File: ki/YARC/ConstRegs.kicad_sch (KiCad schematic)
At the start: 21 parts

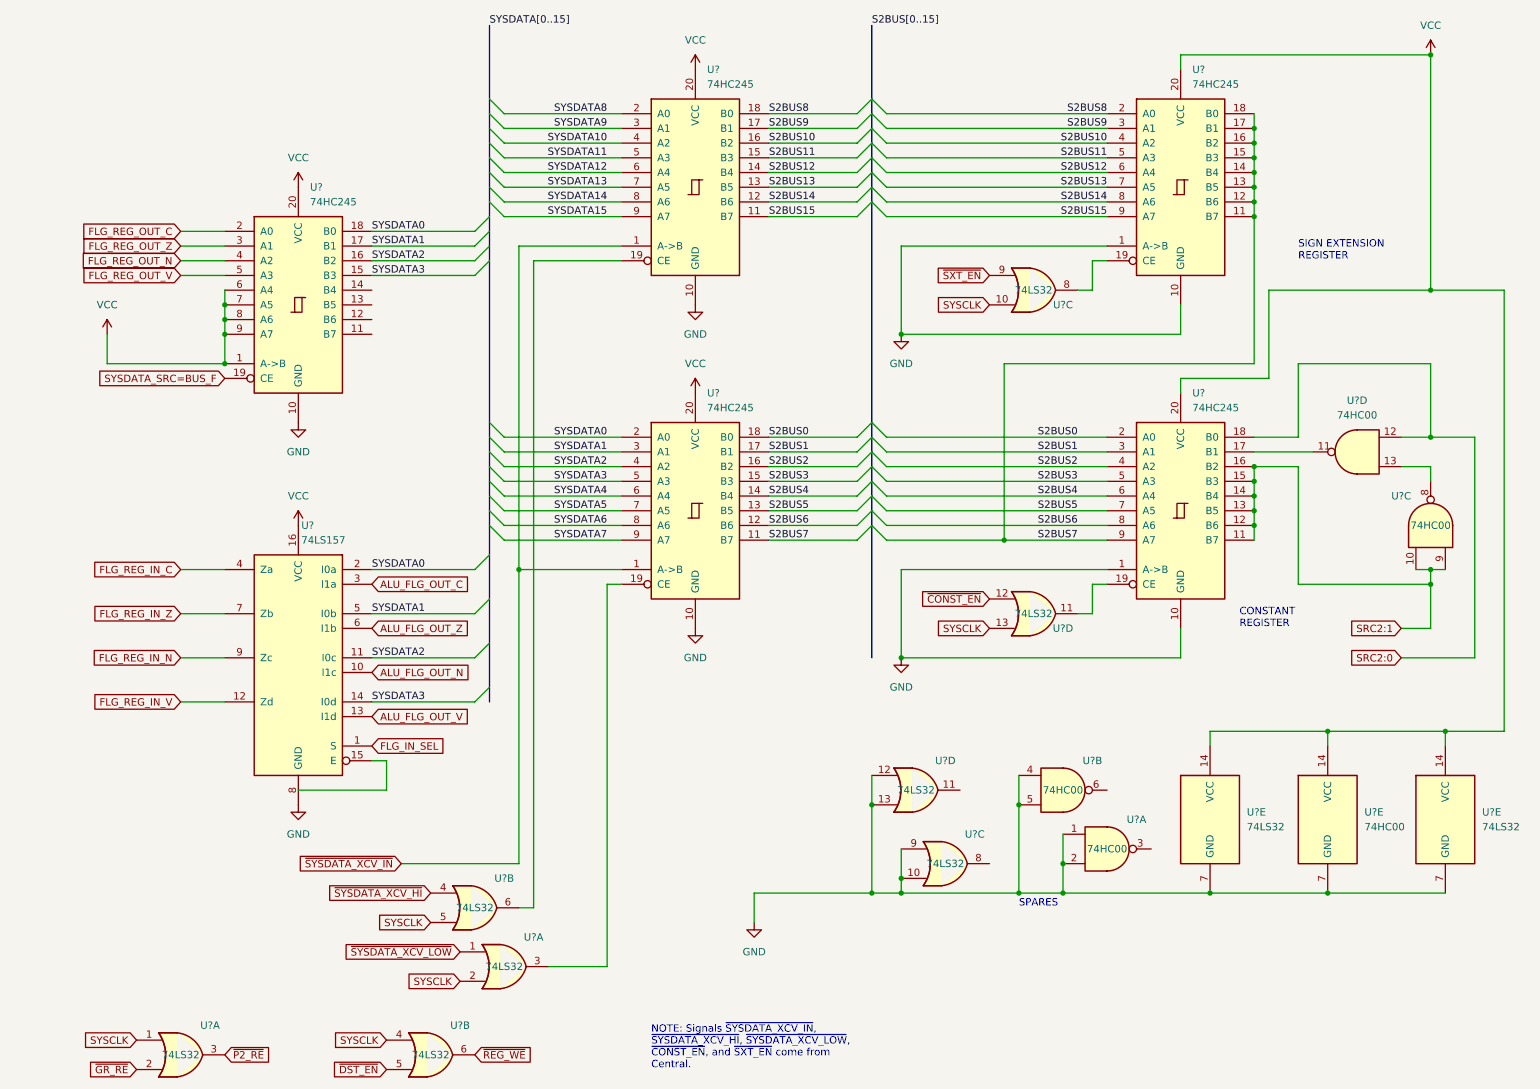
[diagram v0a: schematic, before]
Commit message: Some fixes relating to the bit ordering issue
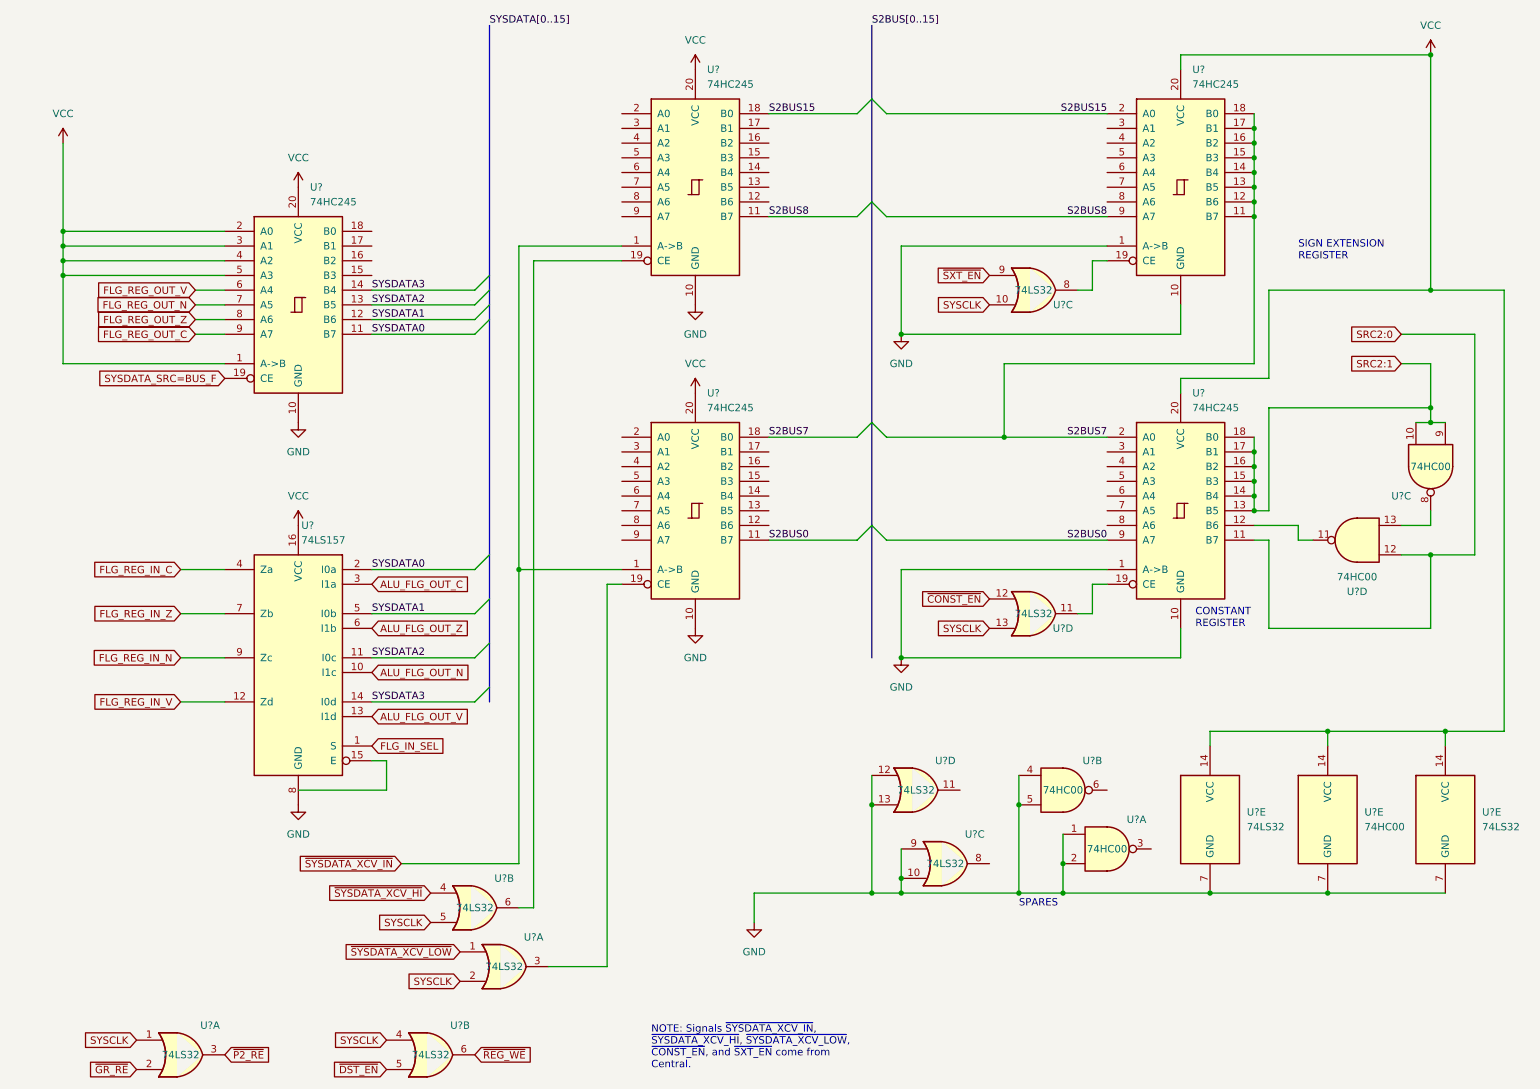
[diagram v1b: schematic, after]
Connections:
- net FLG_REG_OUT_C: now also U?.9 (A7); no longer U?.2 (A0)
- net FLG_REG_OUT_N: now also U?.7 (A5); no longer U?.4 (A2)
- net FLG_REG_OUT_V: now also U?.6 (A4); no longer U?.5 (A3)
- net FLG_REG_OUT_Z: now also U?.8 (A6); no longer U?.3 (A1)
- net S2BUS0: now also U?.11 (B7), U?.9 (A7); no longer U?.18 (B0), U?.2 (A0)
- net S2BUS15: now also U?.18 (B0), U?.2 (A0); no longer U?.11 (B7), U?.9 (A7)
- net S2BUS7: now also U?.18 (B0), U?.2 (A0); no longer U?.11 (B7), U?.9 (A7)
- net S2BUS8: now also U?.11 (B7), U?.9 (A7); no longer U?.18 (B0), U?.2 (A0)
- net SRC2:0: now also U?.11 (B7); no longer U?.18 (B0)
- net SRC2:1: now also U?.17 (B1), U?.18 (B0); no longer U?.11 (B7), U?.12 (B6)
- net SYSDATA0: now also U?.11 (B7); no longer U?.18 (B0), U?.2 (A0)
- net SYSDATA1: now also U?.12 (B6); no longer U?.17 (B1), U?.3 (A1)
- net SYSDATA2: now also U?.13 (B5); no longer U?.16 (B2), U?.4 (A2)
- net SYSDATA3: now also U?.14 (B4); no longer U?.15 (B3), U?.5 (A3)
- net VCC: now also U?.2 (A0), U?.3 (A1), U?.4 (A2), U?.5 (A3); no longer U?.6 (A4), U?.7 (A5), U?.8 (A6), U?.9 (A7)
- net at U?.11: now also U?.12 (B6); no longer U?.17 (B1)
- net S2BUS1: no longer names the net of U?.3 (A1)
- net S2BUS1: no longer U?.17 (B1)
- net S2BUS10: no longer names the net of U?.16 (B2)
- net S2BUS10: no longer U?.4 (A2)
- net S2BUS11: no longer names the net of U?.15 (B3)
- net S2BUS11: no longer U?.5 (A3)
- net S2BUS12: no longer names the net of U?.14 (B4)
- net S2BUS12: no longer U?.6 (A4)
- net S2BUS13: no longer names the net of U?.13 (B5)
- net S2BUS13: no longer U?.7 (A5)
- net S2BUS14: no longer names the net of U?.12 (B6)
- net S2BUS14: no longer U?.8 (A6)
- net S2BUS2: no longer names the net of U?.4 (A2)
- net S2BUS2: no longer U?.16 (B2)
- net S2BUS3: no longer names the net of U?.5 (A3)
- net S2BUS3: no longer U?.15 (B3)
- net S2BUS4: no longer names the net of U?.6 (A4)
- net S2BUS4: no longer U?.14 (B4)
- net S2BUS5: no longer names the net of U?.7 (A5)
- net S2BUS5: no longer U?.13 (B5)
- net S2BUS6: no longer names the net of U?.8 (A6)
- net S2BUS6: no longer U?.12 (B6)
- net S2BUS9: no longer names the net of U?.17 (B1)
- net S2BUS9: no longer U?.3 (A1)
- net SYSDATA10: no longer names the net of U?.4 (A2)
- net SYSDATA11: no longer names the net of U?.5 (A3)
- net SYSDATA12: no longer names the net of U?.6 (A4)
- net SYSDATA13: no longer names the net of U?.7 (A5)
- net SYSDATA14: no longer names the net of U?.8 (A6)
- net SYSDATA15: no longer names the net of U?.9 (A7)
- net SYSDATA4: no longer names the net of U?.6 (A4)
- net SYSDATA5: no longer names the net of U?.7 (A5)
- net SYSDATA6: no longer names the net of U?.8 (A6)
- net SYSDATA7: no longer names the net of U?.9 (A7)
- net SYSDATA8: no longer names the net of U?.2 (A0)
- net SYSDATA9: no longer names the net of U?.3 (A1)
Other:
- moved on the sheet: U?C, U?D

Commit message: Ongoing debugging
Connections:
- net SRC2:0: now also U?.13; no longer U?.12
- net at U?.8: now also U?.12; no longer U?.13
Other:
- moved on the sheet: U?D
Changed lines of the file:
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@@
   (junction (at 15.24 58.42) (diameter 0) (color 0 0 0 0)
   )
+  (junction (at 259.08 106.68) (diameter 0) (color 0 0 0 0)
+  )
   (junction (at 220.98 40.64) (diameter 0) (color 0 0 0 0)
   )
@@
   (junction (at 15.24 53.34) (diameter 0) (color 0 0 0 0)
   )
-  (junction (at 251.46 109.22) (diameter 0) (color 0 0 0 0)
-  )
   (junction (at 233.68 139.7) (diameter 0) (color 0 0 0 0)
   )
@@
     (stroke (width 0) (type default) (color 0 0 0 0))
   )
-  (wire (pts (xy 251.46 121.92) (xy 251.46 109.22))
+  (wire (pts (xy 243.84 106.68) (xy 259.08 106.68))
     (stroke (width 0) (type default) (color 0 0 0 0))
   )
@@
     (stroke (width 0) (type default) (color 0 0 0 0))
   )
-  (wire (pts (xy 228.6 104.14) (xy 220.98 104.14))
-    (stroke (width 0) (type default) (color 0 0 0 0))
-  )
   (wire (pts (xy 223.52 83.82) (xy 251.46 83.82))
     (stroke (width 0) (type default) (color 0 0 0 0))
@@
     (stroke (width 0) (type default) (color 0 0 0 0))
   )
+  (wire (pts (xy 223.52 106.68) (xy 223.52 111.76))
+    (stroke (width 0) (type default) (color 0 0 0 0))
+  )
   (bus (pts (xy 88.9 68.58) (xy 88.9 109.22))
     (stroke (width 0) (type default) (color 0 0 0 0))
@@
     (stroke (width 0) (type default) (color 0 0 0 0))
   )
-  (wire (pts (xy 231.14 106.68) (xy 228.6 106.68))
-    (stroke (width 0) (type default) (color 0 0 0 0))
-  )
   (wire (pts (xy 109.22 180.34) (xy 109.22 114.3))
     (stroke (width 0) (type default) (color 0 0 0 0))
@@
     (stroke (width 0) (type default) (color 0 0 0 0))
   )
-  (wire (pts (xy 223.52 106.68) (xy 223.52 121.92))
-    (stroke (width 0) (type default) (color 0 0 0 0))
-  )
   (wire (pts (xy 220.98 91.44) (xy 220.98 88.9))
     (stroke (width 0) (type default) (color 0 0 0 0))
@@
     (stroke (width 0) (type default) (color 0 0 0 0))
   )
-  (wire (pts (xy 251.46 104.14) (xy 246.38 104.14))
-    (stroke (width 0) (type default) (color 0 0 0 0))
-  )
   (wire (pts (xy 93.98 170.18) (xy 96.52 170.18))
     (stroke (width 0) (type default) (color 0 0 0 0))
@@
     (stroke (width 0) (type default) (color 0 0 0 0))
   )
+  (wire (pts (xy 259.08 106.68) (xy 259.08 111.76))
+    (stroke (width 0) (type default) (color 0 0 0 0))
+  )
   (wire (pts (xy 223.52 78.74) (xy 223.52 63.5))
     (stroke (width 0) (type default) (color 0 0 0 0))
   )
+  (wire (pts (xy 259.08 71.12) (xy 259.08 106.68))
+    (stroke (width 0) (type default) (color 0 0 0 0))
+  )
   (wire (pts (xy 220.98 76.2) (xy 220.98 50.8))
     (stroke (width 0) (type default) (color 0 0 0 0))
@@
     (stroke (width 0) (type default) (color 0 0 0 0))
   )
-  (wire (pts (xy 223.52 121.92) (xy 251.46 121.92))
+  (wire (pts (xy 220.98 104.14) (xy 228.6 104.14))
     (stroke (width 0) (type default) (color 0 0 0 0))
   )
@@
     (stroke (width 0) (type default) (color 0 0 0 0))
   )
-  (wire (pts (xy 251.46 101.6) (xy 251.46 104.14))
-    (stroke (width 0) (type default) (color 0 0 0 0))
-  )
   (wire (pts (xy 180.34 152.4) (xy 180.34 167.64))
     (stroke (width 0) (type default) (color 0 0 0 0))
@@
     (stroke (width 0) (type default) (color 0 0 0 0))
   )
-  (wire (pts (xy 259.08 109.22) (xy 251.46 109.22))
-    (stroke (width 0) (type default) (color 0 0 0 0))
-  )
   (wire (pts (xy 246.38 76.2) (xy 251.46 76.2))
     (stroke (width 0) (type default) (color 0 0 0 0))
@@
     (stroke (width 0) (type default) (color 0 0 0 0))
   )
+  (wire (pts (xy 251.46 101.6) (xy 243.84 101.6))
+    (stroke (width 0) (type default) (color 0 0 0 0))
+  )
   (wire (pts (xy 86.36 71.12) (xy 68.58 71.12))
     (stroke (width 0) (type default) (color 0 0 0 0))
@@
     (stroke (width 0) (type default) (color 0 0 0 0))
   )
+  (wire (pts (xy 223.52 111.76) (xy 259.08 111.76))
+    (stroke (width 0) (type default) (color 0 0 0 0))
+  )
   (wire (pts (xy 220.98 40.64) (xy 220.98 43.18))
     (stroke (width 0) (type default) (color 0 0 0 0))
@@
     (stroke (width 0) (type default) (color 0 0 0 0))
   )
-  (wire (pts (xy 259.08 71.12) (xy 259.08 109.22))
-    (stroke (width 0) (type default) (color 0 0 0 0))
-  )
   (wire (pts (xy 86.36 119.38) (xy 68.58 119.38))
     (stroke (width 0) (type default) (color 0 0 0 0))
@@
     (stroke (width 0) (type default) (color 0 0 0 0))
   )
-  (wire (pts (xy 228.6 106.68) (xy 228.6 104.14))
-    (stroke (width 0) (type default) (color 0 0 0 0))
-  )
   (bus (pts (xy 154.94 17.78) (xy 154.94 30.48))
     (stroke (width 0) (type default) (color 0 0 0 0))
@@
   )
   (wire (pts (xy 160.02 167.64) (xy 180.34 167.64))
-    (stroke (width 0) (type default) (color 0 0 0 0))
-  )
-  (wire (pts (xy 251.46 109.22) (xy 246.38 109.22))
     (stroke (width 0) (type default) (color 0 0 0 0))
   )
@@
   (symbol (lib_id "74xx:74HC00") (at 251.46 93.98 270) (unit 3)
     (in_bom yes) (on_board yes)
-    (property "Reference" "U?" (id 0) (at 246.38 99.06 90))
+    (property "Reference" "U?" (id 0) (at 256.54 99.06 90))
     (property "Value" "74HC00" (id 1) (at 251.46 93.98 90))
     (property "Footprint" "" (id 2) (at 251.46 93.98 0)
@@
     (pin "7")
   )
-  (symbol (lib_id "74xx:74HC00") (at 238.76 106.68 180) (unit 4)
-    (in_bom yes) (on_board yes) (fields_autoplaced)
-    (property "Reference" "U?" (id 0) (at 238.76 115.57 0))
-    (property "Value" "74HC00" (id 1) (at 238.76 113.03 0))
-    (property "Footprint" "" (id 2) (at 238.76 106.68 0)
-      (effects (font (size 1.27 1.27)) hide)
-    )
-    (property "Datasheet" "http://www.ti.com/lit/gpn/sn74hc00" (id 3) (at 238.76 106.68 0)
-      (effects (font (size 1.27 1.27)) hide)
-    )
+  (symbol (lib_id "74xx:74HC00") (at 236.22 104.14 0) (mirror y) (unit 4)
+    (in_bom yes) (on_board yes)
+    (property "Reference" "U?" (id 0) (at 233.68 99.06 0))
+    (property "Value" "74HC00" (id 1) (at 236.22 104.14 0))
+    (property "Footprint" "" (id 2) (at 236.22 104.14 0)
+      (effects (font (size 1.27 1.27)) hide)
+    )
+    (property "Datasheet" "http://www.ti.com/lit/gpn/sn74hc00" (id 3) (at 236.22 104.14 0)
+      (effects (font (size 1.27 1.27)) hide)
+    )

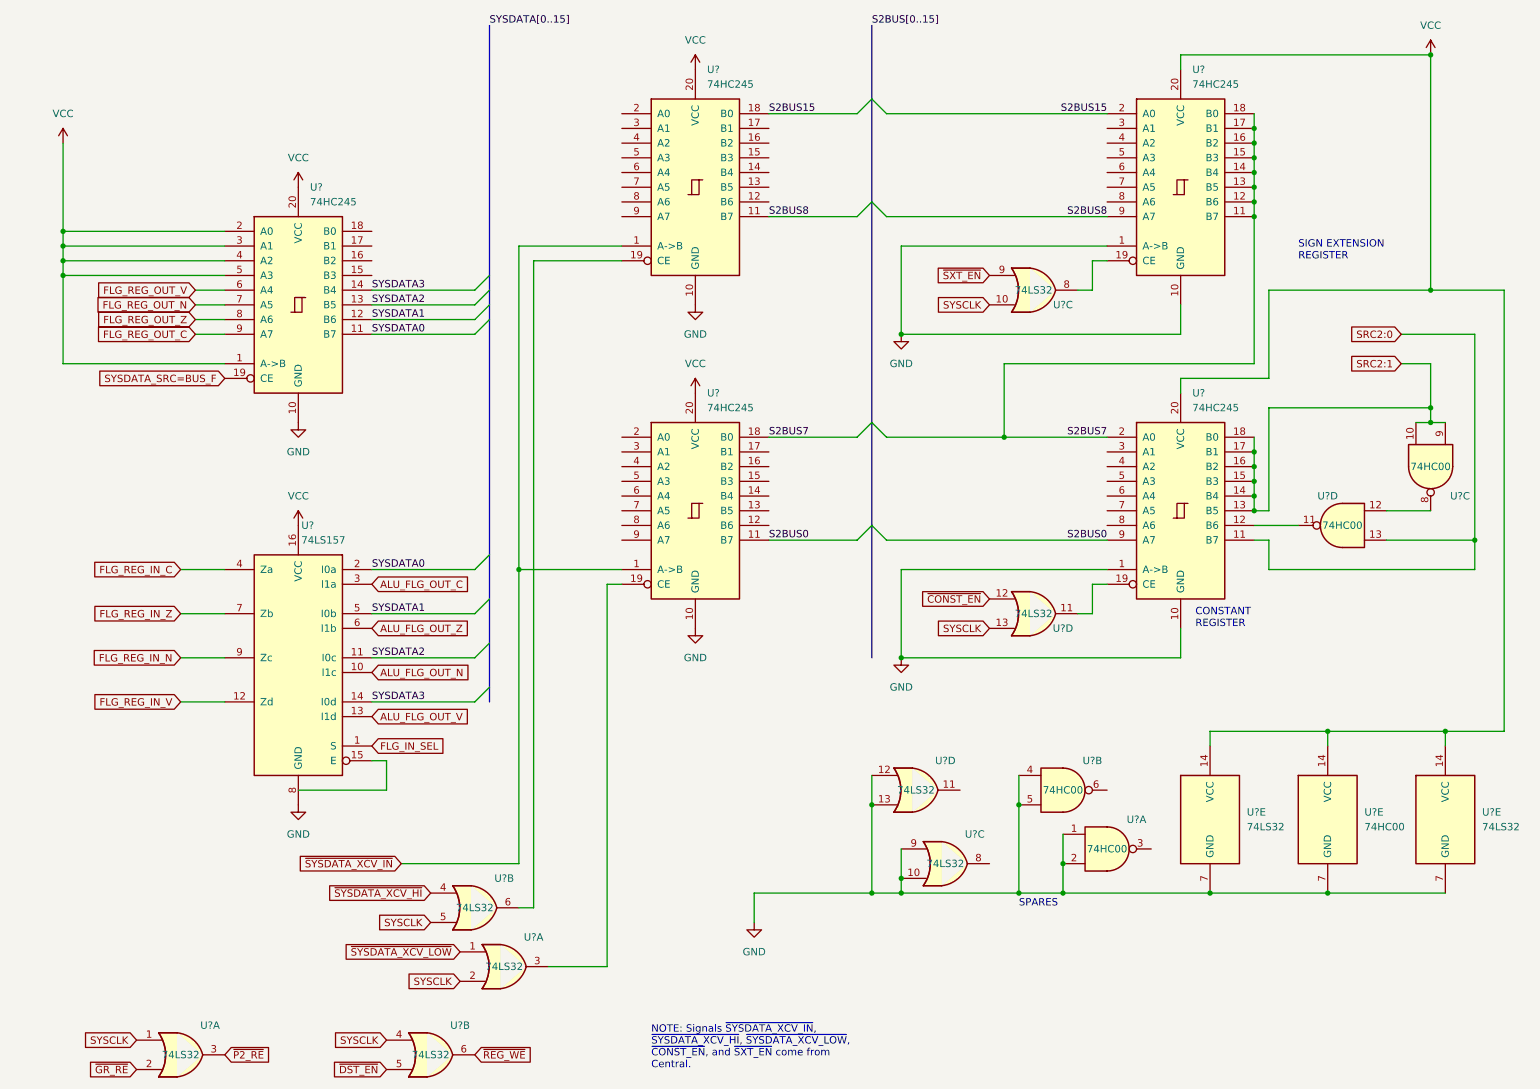
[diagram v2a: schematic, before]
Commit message: Assign part labels (U-numbers) in KiCad and start adding them to Fritzing layouts
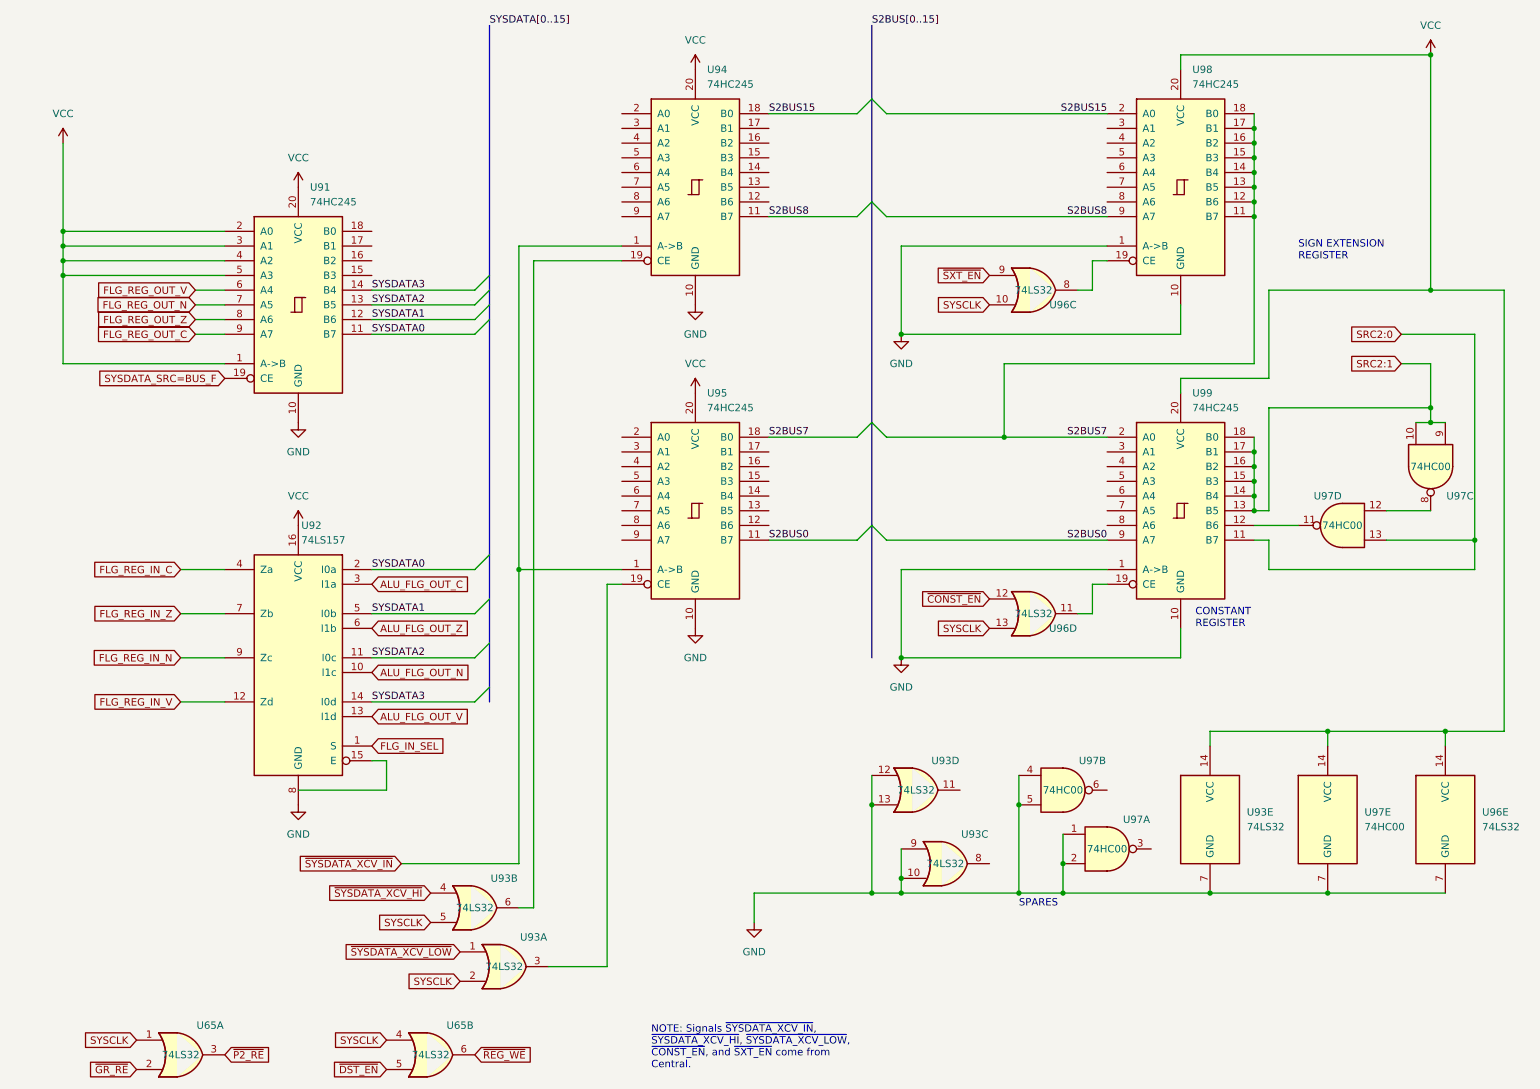
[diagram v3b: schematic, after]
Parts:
- gave numbers to parts that had none: 10
